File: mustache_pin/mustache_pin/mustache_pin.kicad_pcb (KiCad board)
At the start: 2 copper layers, 81 x 60 mm, 8 parts, among them SW1 SW_SPDT

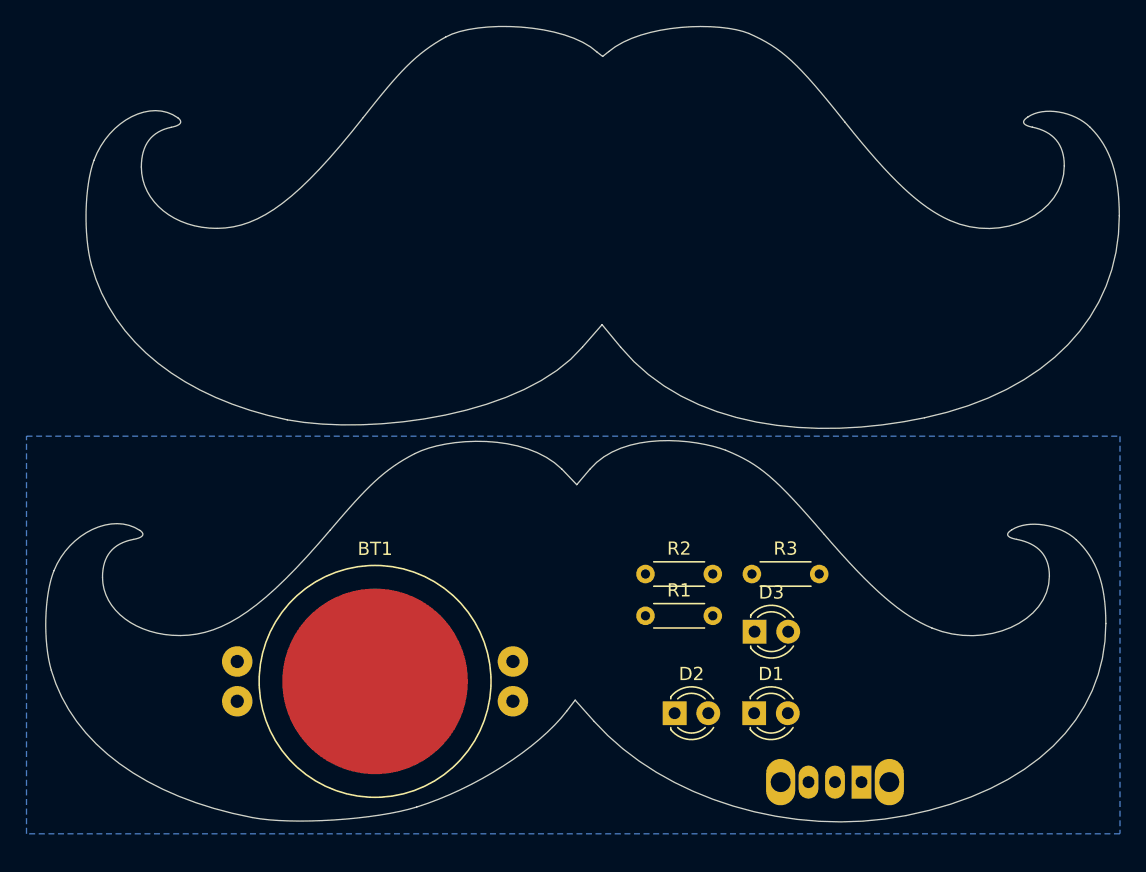
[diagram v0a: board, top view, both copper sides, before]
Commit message: silkscreens are weird
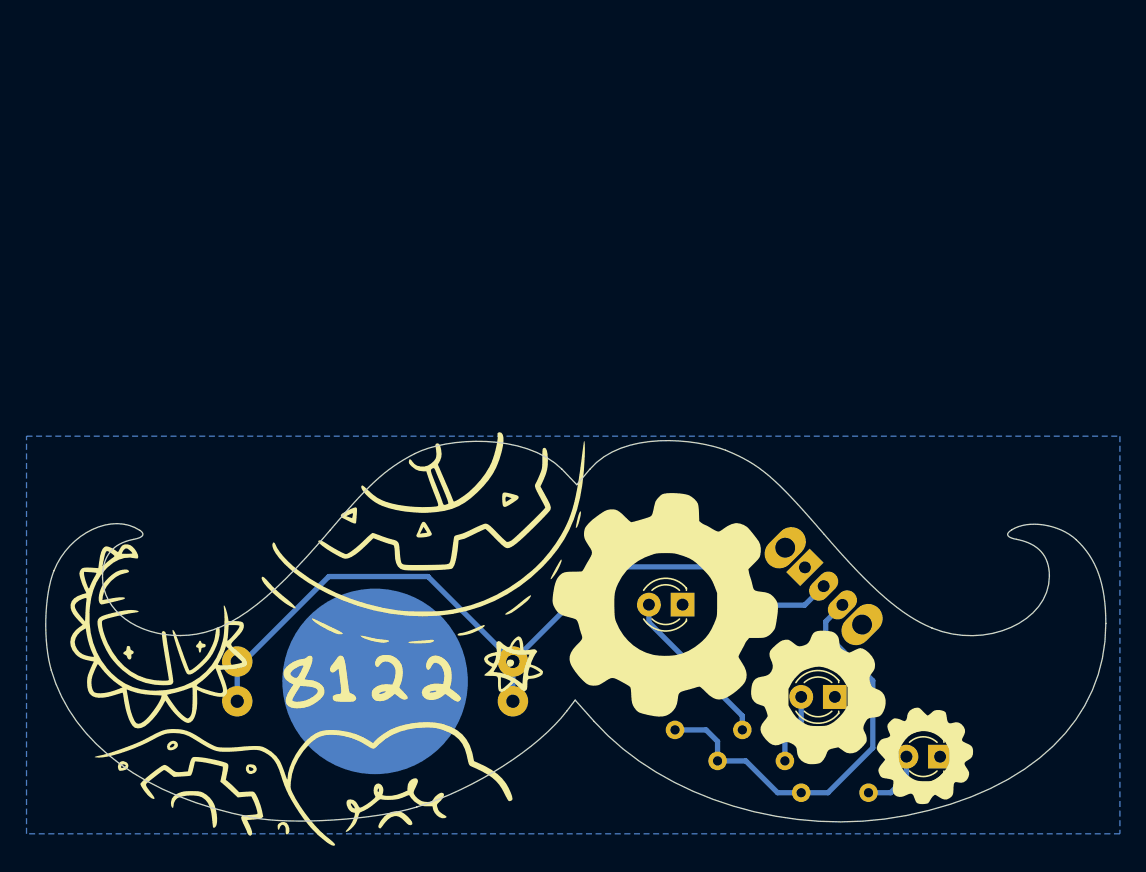
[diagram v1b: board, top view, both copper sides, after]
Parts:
- added G***: LOGO, Symbol:mustache_pin, F.Cu at (202.2, 102.0)
- added G***: LOGO, Symbol:mustache_gears, F.Cu at (208.0, 88.5)
- BT1, R1, R2, R3: moved to B.Cu
- moved R1 21.5 mm to (216.0, 99.4), turned to 180 degrees
- moved R2 17.6 mm to (209.7, 97.0), turned to 180 degrees
- moved SW1 16.8 mm to (211.2, 82.4), turned to -45 degrees
- moved D1 14.4 mm to (221.4, 96.7), turned to 180 degrees
- moved De 12.2 mm to (213.5, 92.2), turned to 180 degrees
- moved R3 11.8 mm to (206.5, 94.7), turned to 180 degrees
- moved D3 5.80 mm to (202.0, 85.2), turned to 180 degrees
- turned BT1 to 180 degrees
- renumbered D2 to De
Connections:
- SW1 pad 1: Net-(R1-Pad2) -> unconnected-(SW1-Pad1)
- SW1 pad 3: unconnected-(SW1-Pad3) -> Net-(R1-Pad2)
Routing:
- net Net-(BT1-Pad1): track 0.00 -> 60.3 mm
- net Net-(R1-Pad2): track 0.00 -> 31.9 mm
- net Net-(D3-Pad2): track 0.00 -> 12.4 mm
- net Net-(D2-Pad2): track 0.00 -> 5.34 mm
- net Net-(D1-Pad2): track 0.00 -> 4.88 mm
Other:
- board size 81 x 60 mm -> 80 x 28.8 mm

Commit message: commit pt2
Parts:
- removed the G*** at (202.2, 102.0)
- added G***: LOGO, Symbol:mustache name, F.Cu at (201.0, 102.0)
